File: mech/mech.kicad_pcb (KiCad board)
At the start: 2 copper layers, 66 x 120.7 mm, 50 parts, among them P1 Pump_Motor_DC, P2 Pump_Motor_DC, T1 DS18B20, T2 DS18B20, U1 DHT22, U2 PCA9685PW, U3 ADC128D818, U4 ADC128D818

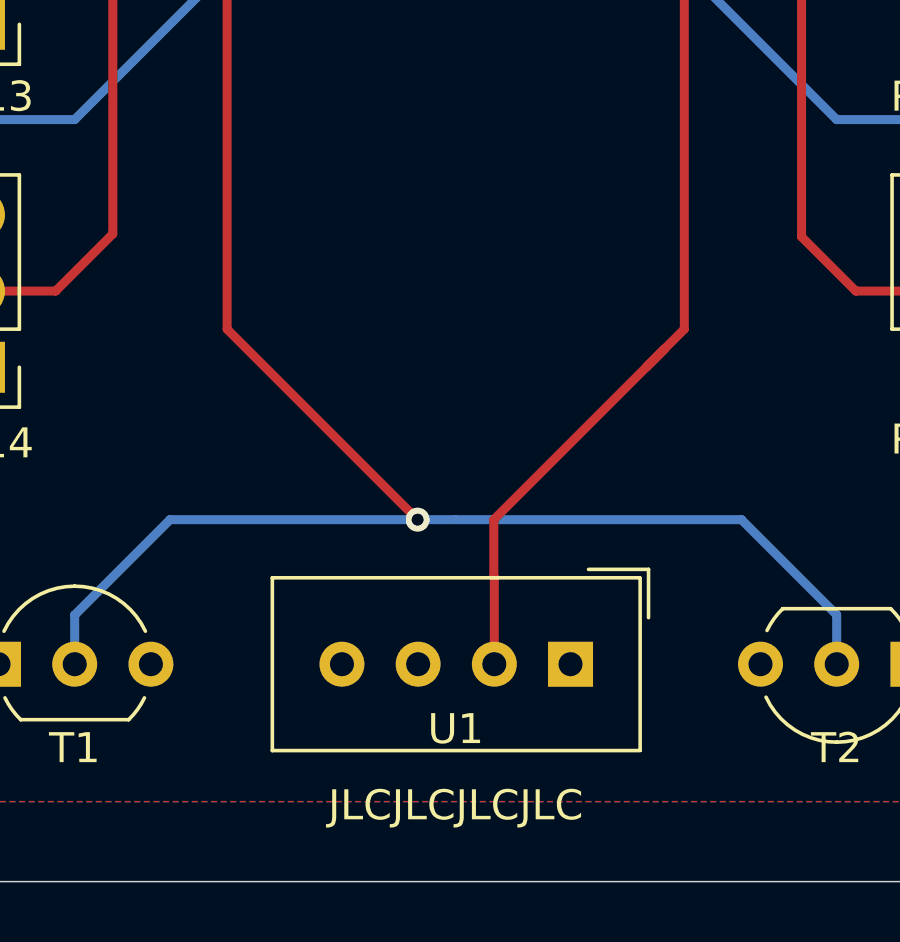
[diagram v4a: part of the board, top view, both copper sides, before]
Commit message: add JLC id placeholder
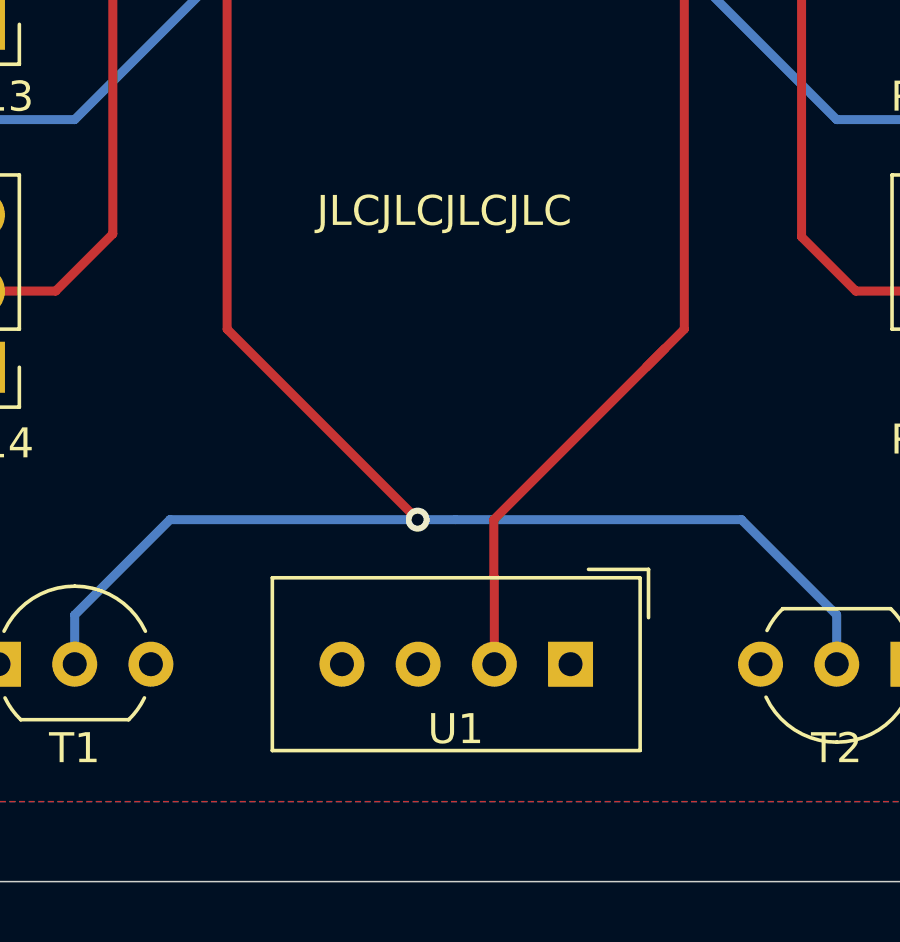
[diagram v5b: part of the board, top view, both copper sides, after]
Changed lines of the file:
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@@
   )
   (setup
-    (last_trace_width 0.3)
+    (last_trace_width 0.25)
     (user_trace_width 0.3)
     (user_trace_width 0.5)
@@
     (add_net I2C-SCL)
     (add_net I2C-SDA)
-    (add_net "Net-(DSUB1-Pad3)")
     (add_net "Net-(M-1-Pad1)")
     (add_net "Net-(M-10-Pad1)")
@@
     (add_net "Net-(RV8-Pad2)")
     (add_net "Net-(RV9-Pad2)")
-    (add_net "Net-(T2-Pad3)")
-    (add_net "Net-(U1-Pad3)")
-    (add_net "Net-(U2-Pad15)")
-    (add_net "Net-(U2-Pad6)")
-    (add_net "Net-(U3-Pad16)")
-    (add_net "Net-(U3-Pad6)")
-    (add_net "Net-(U4-Pad16)")
-    (add_net "Net-(U4-Pad6)")
     (add_net Pump-1)
     (add_net Pump-2)
@@
     (effects (font (size 1 1) (thickness 0.15)) (justify mirror))
   )
-  (gr_text JLCJLCJLCJLC (at 101.6 213.36) (layer F.SilkS)
+  (gr_text JLCJLCJLCJLC (at 101.219 193.548) (layer F.SilkS)
     (effects (font (size 1 1) (thickness 0.15)))
   )
@@
   (segment (start 118.11 113.03) (end 122.555 113.03) (width 1) (layer B.Cu) (net 22))
   (segment (start 110.49 105.41) (end 118.11 113.03) (width 1) (layer B.Cu) (net 22))
-  (segment (start 90.48 167.315) (end 92.3 167.315) (width 0.3) (layer F.Cu) (net 33))
-  (segment (start 88.9 162.56) (end 88.9 165.735) (width 0.3) (layer F.Cu) (net 33))
-  (segment (start 85.725 161.925) (end 88.265 161.925) (width 0.3) (layer F.Cu) (net 33))
-  (segment (start 88.9 165.735) (end 90.48 167.315) (width 0.3) (layer F.Cu) (net 33))
-  (segment (start 88.265 161.925) (end 88.9 162.56) (width 0.3) (layer F.Cu) (net 33))
-  (segment (start 90.59424 169.265) (end 92.3 169.265) (width 0.3) (layer F.Cu) (net 36))
-  (segment (start 90.17 194.31) (end 90.17 169.68924) (width 0.3) (layer F.Cu) (net 36))
-  (segment (start 90.17 169.68924) (end 90.59424 169.265) (width 0.3) (layer F.Cu) (net 36))
-  (segment (start 85.725 196.215) (end 88.265 196.215) (width 0.3) (layer F.Cu) (net 36))
-  (segment (start 88.265 196.215) (end 90.17 194.31) (width 0.3) (layer F.Cu) (net 36))
-  (segment (start 89.535 169.61712) (end 90.53712 168.615) (width 0.3) (layer F.Cu) (net 35))
-  (segment (start 85.725 184.785) (end 88.265 184.785) (width 0.3) (layer F.Cu) (net 35))
-  (segment (start 90.53712 168.615) (end 92.3 168.615) (width 0.3) (layer F.Cu) (net 35))
-  (segment (start 89.535 183.515) (end 89.535 169.61712) (width 0.3) (layer F.Cu) (net 35))
-  (segment (start 88.265 184.785) (end 89.535 183.515) (width 0.3) (layer F.Cu) (net 35))
-  (segment (start 90.48 167.965) (end 92.3 167.965) (width 0.3) (layer F.Cu) (net 34))
-  (segment (start 85.725 173.355) (end 88.265 173.355) (width 0.3) (layer F.Cu) (net 34))
-  (segment (start 88.9 169.545) (end 90.48 167.965) (width 0.3) (layer F.Cu) (net 34))
-  (segment (start 88.9 172.72) (end 88.9 169.545) (width 0.3) (layer F.Cu) (net 34))
-  (segment (start 88.265 173.355) (end 88.9 172.72) (width 0.3) (layer F.Cu) (net 34))
   (segment (start 110.974999 165.454999) (end 110.9 165.38) (width 0.3) (layer F.Cu) (net 23))
   (segment (start 111.930001 165.454999) (end 110.974999 165.454999) (width 0.3) (layer F.Cu) (net 23))
@@
   (segment (start 112.705 167.33) (end 114.3 165.735) (width 0.3) (layer F.Cu) (net 26))
   (segment (start 110.9 167.33) (end 112.705 167.33) (width 0.3) (layer F.Cu) (net 26))
-  (segment (start 89.535 151.765) (end 89.535 165.66288) (width 0.3) (layer F.Cu) (net 32))
-  (segment (start 90.53712 166.665) (end 92.3 166.665) (width 0.3) (layer F.Cu) (net 32))
-  (segment (start 89.535 165.66288) (end 90.53712 166.665) (width 0.3) (layer F.Cu) (net 32))
-  (segment (start 85.725 150.495) (end 88.265 150.495) (width 0.3) (layer F.Cu) (net 32))
-  (segment (start 88.265 150.495) (end 89.535 151.765) (width 0.3) (layer F.Cu) (net 32))
-  (segment (start 90.59424 166.015) (end 92.3 166.015) (width 0.3) (layer F.Cu) (net 31))
-  (segment (start 90.17 165.59076) (end 90.59424 166.015) (width 0.3) (layer F.Cu) (net 31))
-  (segment (start 90.17 140.97) (end 90.17 165.59076) (width 0.3) (layer F.Cu) (net 31))
-  (segment (start 85.725 139.065) (end 88.265 139.065) (width 0.3) (layer F.Cu) (net 31))
-  (segment (start 88.265 139.065) (end 90.17 140.97) (width 0.3) (layer F.Cu) (net 31))
-  (segment (start 91.07 165.365) (end 92.3 165.365) (width 0.3) (layer F.Cu) (net 30))
-  (segment (start 90.67001 164.96501) (end 91.07 165.365) (width 0.3) (layer F.Cu) (net 30))
-  (segment (start 85.725 127.635) (end 88.265 127.635) (width 0.3) (layer F.Cu) (net 30))
-  (segment (start 90.67001 130.04001) (end 90.67001 164.96501) (width 0.3) (layer F.Cu) (net 30))
-  (segment (start 88.265 127.635) (end 90.67001 130.04001) (width 0.3) (layer F.Cu) (net 30))
   (segment (start 114.3 172.72) (end 114.3 169.545) (width 0.3) (layer F.Cu) (net 27))
   (segment (start 114.935 173.355) (end 114.3 172.72) (width 0.3) (layer F.Cu) (net 27))
@@
   (segment (start 113.12893 169.78817) (end 113.12893 194.40893) (width 0.3) (layer F.Cu) (net 29))
   (segment (start 112.62076 169.28) (end 113.12893 169.78817) (width 0.3) (layer F.Cu) (net 29))
+  (segment (start 91.07 165.365) (end 92.3 165.365) (width 0.3) (layer F.Cu) (net 30))
+  (segment (start 90.67001 164.96501) (end 91.07 165.365) (width 0.3) (layer F.Cu) (net 30))
+  (segment (start 85.725 127.635) (end 88.265 127.635) (width 0.3) (layer F.Cu) (net 30))
+  (segment (start 90.67001 130.04001) (end 90.67001 164.96501) (width 0.3) (layer F.Cu) (net 30))
+  (segment (start 88.265 127.635) (end 90.67001 130.04001) (width 0.3) (layer F.Cu) (net 30))
+  (segment (start 90.59424 166.015) (end 92.3 166.015) (width 0.3) (layer F.Cu) (net 31))
+  (segment (start 90.17 165.59076) (end 90.59424 166.015) (width 0.3) (layer F.Cu) (net 31))
+  (segment (start 90.17 140.97) (end 90.17 165.59076) (width 0.3) (layer F.Cu) (net 31))
+  (segment (start 85.725 139.065) (end 88.265 139.065) (width 0.3) (layer F.Cu) (net 31))
+  (segment (start 88.265 139.065) (end 90.17 140.97) (width 0.3) (layer F.Cu) (net 31))
+  (segment (start 89.535 151.765) (end 89.535 165.66288) (width 0.3) (layer F.Cu) (net 32))
+  (segment (start 90.53712 166.665) (end 92.3 166.665) (width 0.3) (layer F.Cu) (net 32))
+  (segment (start 89.535 165.66288) (end 90.53712 166.665) (width 0.3) (layer F.Cu) (net 32))
+  (segment (start 85.725 150.495) (end 88.265 150.495) (width 0.3) (layer F.Cu) (net 32))
+  (segment (start 88.265 150.495) (end 89.535 151.765) (width 0.3) (layer F.Cu) (net 32))
+  (segment (start 90.48 167.315) (end 92.3 167.315) (width 0.3) (layer F.Cu) (net 33))
+  (segment (start 88.9 162.56) (end 88.9 165.735) (width 0.3) (layer F.Cu) (net 33))
+  (segment (start 85.725 161.925) (end 88.265 161.925) (width 0.3) (layer F.Cu) (net 33))
+  (segment (start 88.9 165.735) (end 90.48 167.315) (width 0.3) (layer F.Cu) (net 33))
+  (segment (start 88.265 161.925) (end 88.9 162.56) (width 0.3) (layer F.Cu) (net 33))
+  (segment (start 90.48 167.965) (end 92.3 167.965) (width 0.3) (layer F.Cu) (net 34))
+  (segment (start 85.725 173.355) (end 88.265 173.355) (width 0.3) (layer F.Cu) (net 34))
+  (segment (start 88.9 169.545) (end 90.48 167.965) (width 0.3) (layer F.Cu) (net 34))
+  (segment (start 88.9 172.72) (end 88.9 169.545) (width 0.3) (layer F.Cu) (net 34))
+  (segment (start 88.265 173.355) (end 88.9 172.72) (width 0.3) (layer F.Cu) (net 34))
+  (segment (start 89.535 169.61712) (end 90.53712 168.615) (width 0.3) (layer F.Cu) (net 35))
+  (segment (start 85.725 184.785) (end 88.265 184.785) (width 0.3) (layer F.Cu) (net 35))
+  (segment (start 90.53712 168.615) (end 92.3 168.615) (width 0.3) (layer F.Cu) (net 35))
+  (segment (start 89.535 183.515) (end 89.535 169.61712) (width 0.3) (layer F.Cu) (net 35))
+  (segment (start 88.265 184.785) (end 89.535 183.515) (width 0.3) (layer F.Cu) (net 35))
+  (segment (start 90.59424 169.265) (end 92.3 169.265) (width 0.3) (layer F.Cu) (net 36))
+  (segment (start 90.17 194.31) (end 90.17 169.68924) (width 0.3) (layer F.Cu) (net 36))
+  (segment (start 90.17 169.68924) (end 90.59424 169.265) (width 0.3) (layer F.Cu) (net 36))
+  (segment (start 85.725 196.215) (end 88.265 196.215) (width 0.3) (layer F.Cu) (net 36))
+  (segment (start 88.265 196.215) (end 90.17 194.31) (width 0.3) (layer F.Cu) (net 36))
   (zone (net 1) (net_name +5V) (layer F.Cu) (hatch edge 0.508)
     (connect_pads (clearance 0.508))

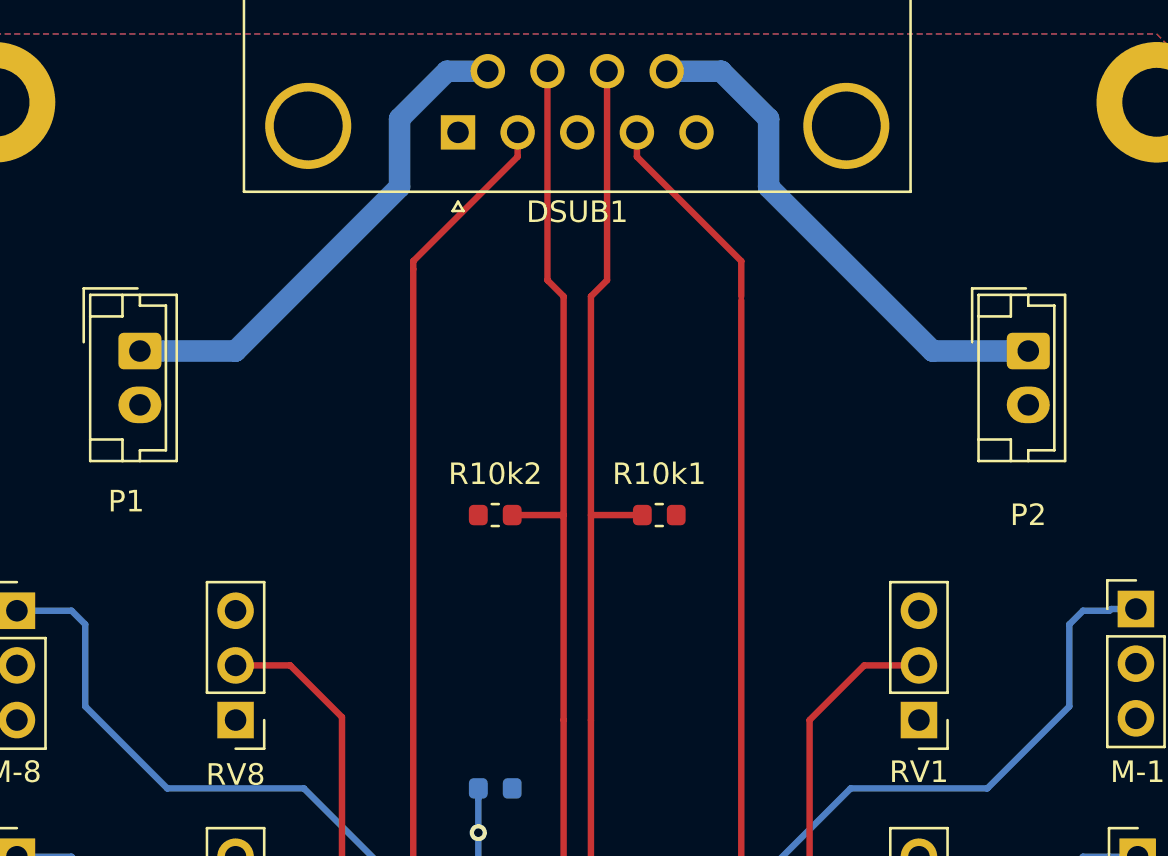
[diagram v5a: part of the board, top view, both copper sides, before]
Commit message: move mosfet to mech board, controll pump via gnd
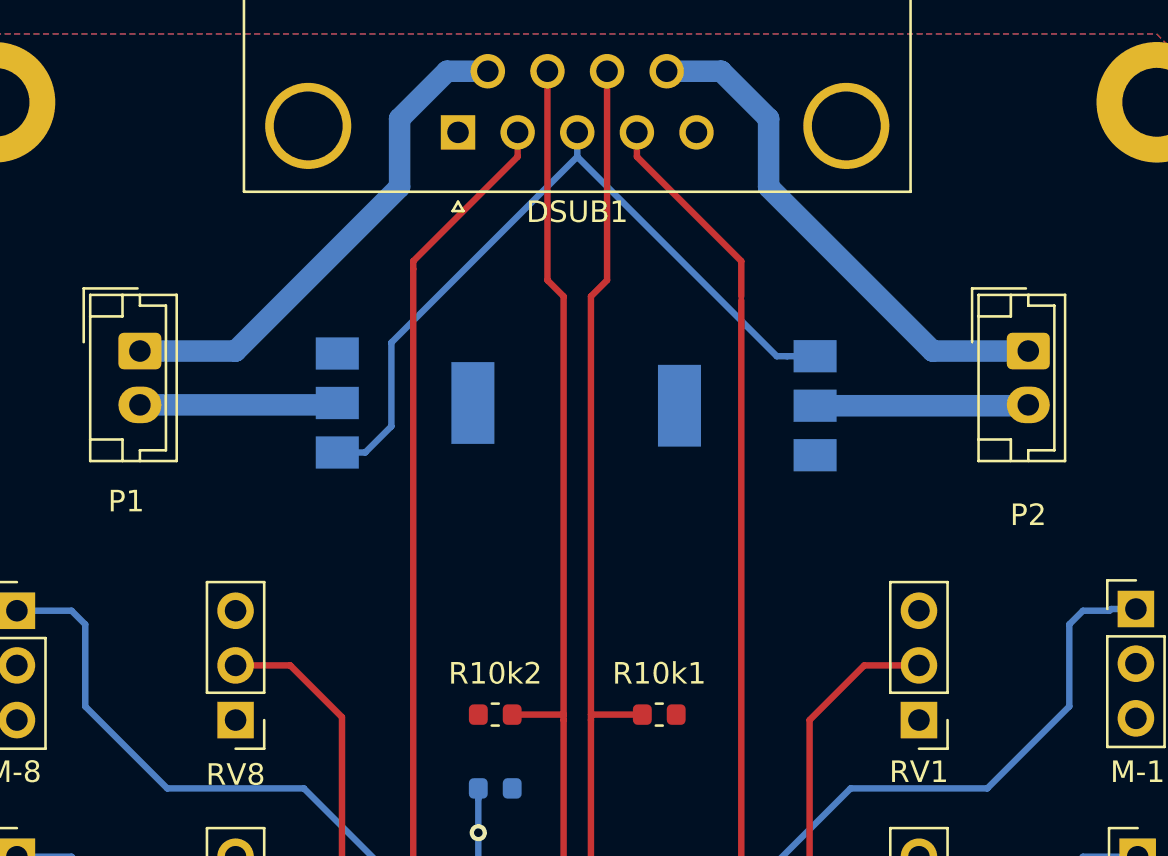
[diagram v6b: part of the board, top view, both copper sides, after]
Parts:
- added U5: IRFL210, Package_TO_SOT_SMD:SOT-223, B.Cu at (109.5, 115.6)
- added U6: IRFL210, Package_TO_SOT_SMD:SOT-223, B.Cu at (93.6, 115.4)
- moved R10k1 9.27 mm to (105.4, 129.9)
- moved R10k2 9.27 mm to (97.8, 129.9)
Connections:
- DSUB1 pad 3: (no net) -> Pump
- DSUB1 pad 6: Pump-2 -> +12V
- DSUB1 pad 9: Pump-1 -> +12V
- P1 pad 1: Pump-2 -> +12V
- P1 pad 2: GND -> Net-(P1-Pad2)
- P2 pad 1: Pump-1 -> +12V
- P2 pad 2: GND -> Net-(P2-Pad2)
- T2 pad 3: (no net) -> Net-(T2-Pad3)
- U1 pad 3: (no net) -> Net-(U1-Pad3)
- U2 pad 15: (no net) -> Net-(U2-Pad15)
- U2 pad 6: (no net) -> Net-(U2-Pad6)
- U3 pad 16: (no net) -> Net-(U3-Pad16)
- U3 pad 6: (no net) -> Net-(U3-Pad6)
- U4 pad 16: (no net) -> Net-(U4-Pad16)
- U4 pad 6: (no net) -> Net-(U4-Pad6)
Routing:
- net +12V: track 0.00 -> 47.5 mm
- net Pump: track 0.00 -> 35.1 mm
- net Pump-1: track 24.0 -> 0.00 mm
- net Pump-2: track 23.4 -> 0.00 mm
- net Net-(P2-Pad2): track 0.00 -> 9.92 mm
- net Net-(P1-Pad2): track 0.00 -> 9.21 mm

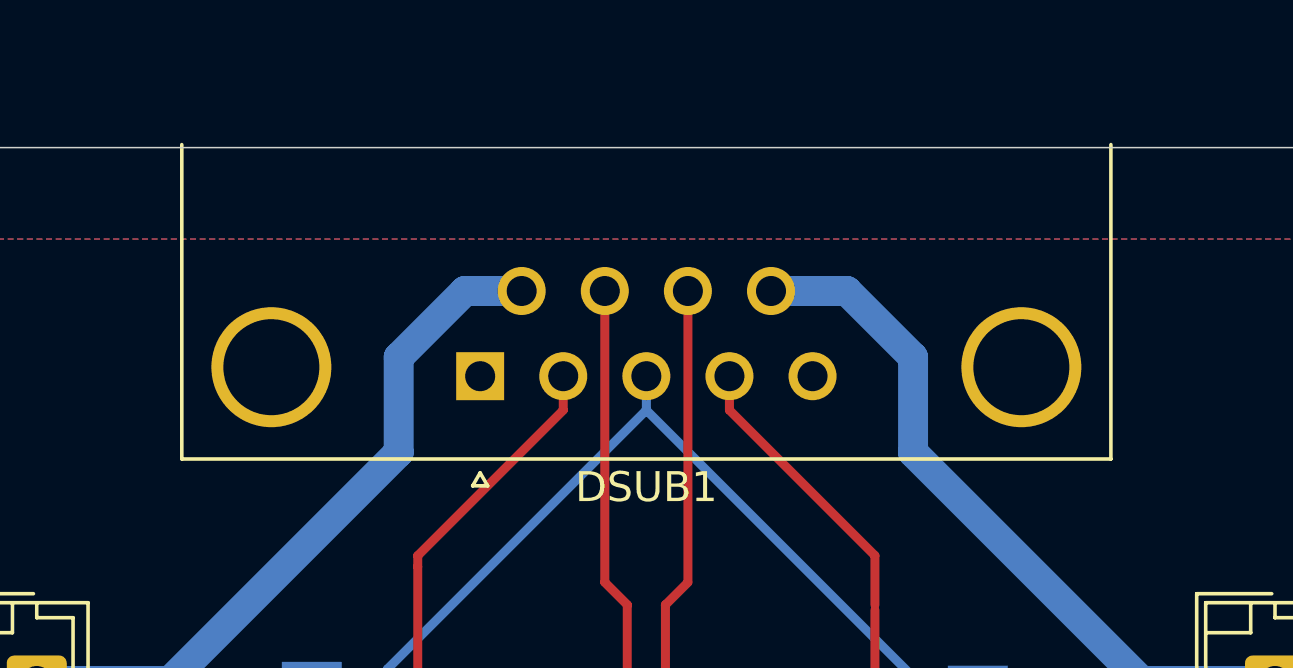
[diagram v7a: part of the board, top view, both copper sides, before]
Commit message: add db9 models, and update footprints
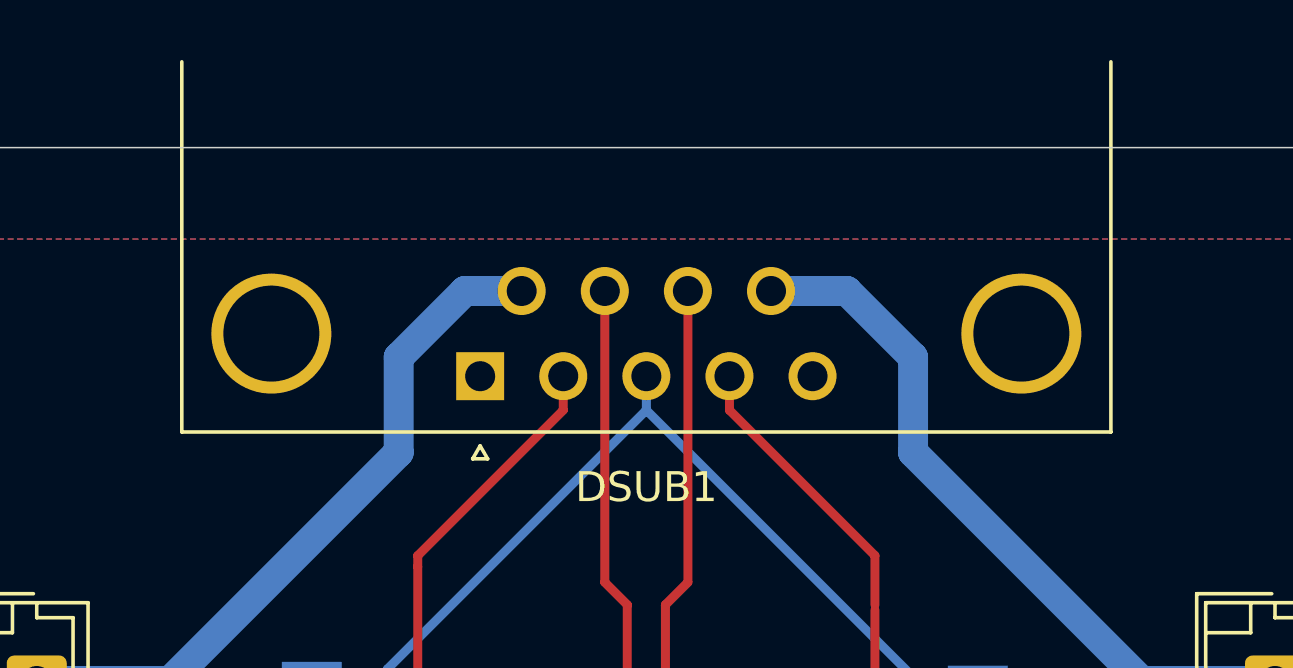
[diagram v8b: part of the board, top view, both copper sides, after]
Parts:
- DSUB1: footprint Connector_Dsub:DSUB-9_Female_Horizontal_P2.77x2.84mm_EdgePinOffset4.94mm_Housed_MountingHolesOffset7.48mm -> Connector_Dsub:DSUB-9_Female_Horizontal_P2.77x2.84mm_EdgePinOffset7.70mm_Housed_MountingHolesOffset9.12mm
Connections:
- DSUB1 pad 3: Pump -> Pump-1-2
